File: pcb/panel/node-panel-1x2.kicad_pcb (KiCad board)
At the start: 4 copper layers, 64 x 108 mm, 325 parts, among them J1 LCD, J10 SPI, J13 Power, J14 SERIAL, J2 USB_C_USB2.0_16P, J3 INDICATOR, J4 GPB[0..3], J5 GPB[4..7], J7 GPA[4..7], J8 QWIIC1, J9 QWIIC2, Q1 MMBT2222A, SW1 RESET, SW2 BOOT, U1 ESP32-S3-WROOM-1-N8R2, U2 LM66200DRLR, U3 USBLC6-2P6, U4 MCP23017_ML, U5 LD1117S33TR_SOT223

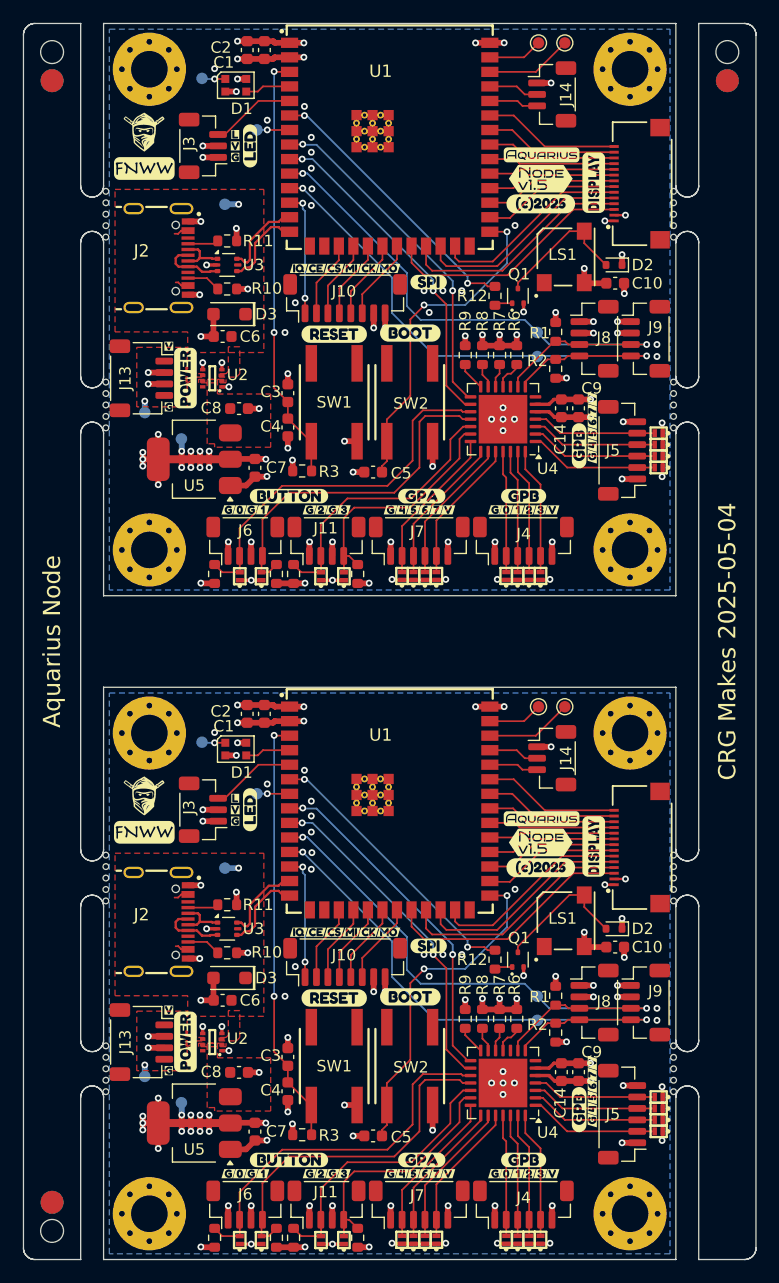
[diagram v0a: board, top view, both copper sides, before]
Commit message: Change panel to be 1x1
Changed connectors be vertical rather than horizontal.
Updated TVS diodes to DFN1006 rather than SMF
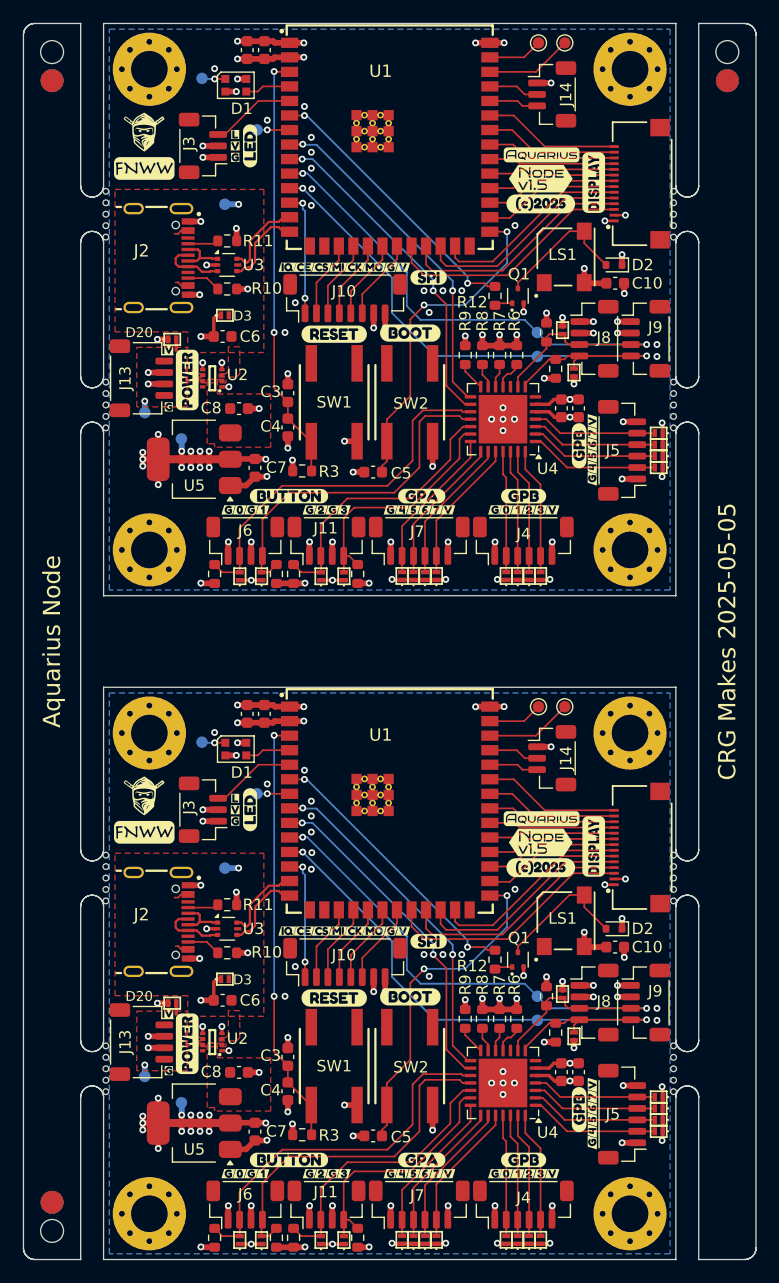
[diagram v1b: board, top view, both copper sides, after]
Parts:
- removed the D3 at (134.5, 45.4)
- removed the D3 at (134.5, 103.4)
- removed the R1 at (163.0, 47.0)
- removed the R1 at (163.0, 105.0)
- removed the kibuzzard-67B9F9C2 at (164.0, 46.7)
- removed the kibuzzard-67B9F9C2 at (164.0, 104.7)
- removed the kibuzzard-67B9F9CD at (164.0, 48.9)
- removed the kibuzzard-67B9F9CD at (164.0, 106.9)
- removed the kibuzzard-680D01D7 at (151.9, 42.6)
- removed the kibuzzard-680D01D7 at (151.9, 100.6)
- removed the kibuzzard-68103456 at (132.4, 26.3)
- removed the kibuzzard-68103456 at (132.4, 84.3)
- removed the kibuzzard-6810346D at (140.3, 27.9)
- removed the kibuzzard-6810346D at (140.3, 85.9)
- removed the kibuzzard-6810349E at (134.3, 34.4)
- removed the kibuzzard-6810349E at (134.3, 92.4)
- removed the kibuzzard-681034B6 at (130.4, 112.0)
- removed the kibuzzard-681034B6 at (130.4, 54.0)
- removed the kibuzzard-681035B7 at (133.1, 113.8)
- removed the kibuzzard-681035B7 at (133.1, 55.8)
- removed the kibuzzard-6812E37E at (142.1, 41.4)
- removed the kibuzzard-6812E37E at (142.1, 99.4)
- removed the kibuzzard-6812E3A0 at (143.7, 41.4)
- removed the kibuzzard-6812E3A0 at (143.7, 99.4)
- removed the kibuzzard-6812E3AD at (145.2, 99.4)
- removed the kibuzzard-6812E3AD at (145.2, 41.4)
- removed the kibuzzard-6812E3BB at (146.7, 41.4)
- removed the kibuzzard-6812E3BB at (146.7, 99.4)
- removed the kibuzzard-6812E3C5 at (148.4, 99.4)
- removed the kibuzzard-6812E3C5 at (148.4, 41.4)
- removed the kibuzzard-6812E420 at (140.6, 41.4)
- removed the kibuzzard-6812E420 at (140.6, 99.4)
- removed the kibuzzard-68142030 at (166.2, 111.8)
- removed the kibuzzard-68142030 at (166.2, 53.9)
- removed the kibuzzard-68142039 at (166.2, 112.8)
- removed the kibuzzard-68142039 at (166.2, 54.9)
- removed the kibuzzard-68142043 at (166.2, 113.8)
- removed the kibuzzard-68142043 at (166.2, 55.9)
- removed the kibuzzard-6814204F at (166.2, 56.9)
- removed the kibuzzard-6814204F at (166.2, 114.8)
- removed the kibuzzard-6814216F at (129.2, 106.2)
- removed the kibuzzard-6814216F at (129.2, 48.2)
- removed the kibuzzard-6815408B at (166.2, 115.8)
- removed the kibuzzard-6815408B at (166.2, 57.9)
- removed the kibuzzard-68154095 at (166.2, 110.8)
- removed the kibuzzard-68154095 at (166.2, 52.8)
- added D20: PESD5V5C1BL, CRGM Passive:DFN1006-2, F.Cu at (129.5, 105.6)
- added D20: PESD5V5C1BL, CRGM Passive:DFN1006-2, F.Cu at (129.5, 47.6)
- added D21: PESD3V3S1BL, CRGM Passive:DFN1006-2, F.Cu at (164.6, 50.5)
- added D21: PESD3V3S1BL, CRGM Passive:DFN1006-2, F.Cu at (164.6, 108.5)
- added D22: PESD3V3S1BL, CRGM Passive:DFN1006-2, F.Cu at (163.6, 46.8)
- added D22: PESD3V3S1BL, CRGM Passive:DFN1006-2, F.Cu at (163.6, 104.8)
- added D3: PESD5V5C1BL, CRGM Passive:DFN1006-2, F.Cu at (134.1, 45.5)
- added D3: PESD5V5C1BL, CRGM Passive:DFN1006-2, F.Cu at (134.1, 103.5)
- added R1: 10K, Resistor_SMD:R_0603_1608Metric, F.Cu at (162.2, 47.0)
- added R1: 10K, Resistor_SMD:R_0603_1608Metric, F.Cu at (162.2, 105.0)
- added kibuzzard-67B9F9C2: G***, kibuzzard-67B9F9C2, B.Cu at (164.1, 47.0)
- added kibuzzard-67B9F9C2: G***, kibuzzard-67B9F9C2, B.Cu at (164.1, 105.0)
- added kibuzzard-67B9F9CD: G***, kibuzzard-67B9F9CD, B.Cu at (163.9, 107.1)
- added kibuzzard-67B9F9CD: G***, kibuzzard-67B9F9CD, B.Cu at (163.9, 49.1)
- added kibuzzard-680D01D7: G***, kibuzzard-680D01D7, F.Cu at (151.9, 100.2)
- added kibuzzard-680D01D7: G***, kibuzzard-680D01D7, F.Cu at (151.9, 42.2)
- added kibuzzard-68103456: G***, kibuzzard-68103456, B.Cu at (132.1, 84.3)
- added kibuzzard-68103456: G***, kibuzzard-68103456, B.Cu at (132.1, 26.3)
- added kibuzzard-6810346D: G***, kibuzzard-6810346D, B.Cu at (134.8, 29.3)
- added kibuzzard-6810346D: G***, kibuzzard-6810346D, B.Cu at (134.8, 87.3)
- added kibuzzard-6810349E: G***, kibuzzard-6810349E, B.Cu at (134.1, 34.4)
- added kibuzzard-6810349E: G***, kibuzzard-6810349E, B.Cu at (134.1, 92.4)
- added kibuzzard-681034B6: G***, kibuzzard-681034B6, B.Cu at (130.1, 112.0)
- added kibuzzard-681034B6: G***, kibuzzard-681034B6, B.Cu at (130.1, 54.0)
- added kibuzzard-681035B7: G***, kibuzzard-681035B7, B.Cu at (132.8, 56.4)
- added kibuzzard-681035B7: G***, kibuzzard-681035B7, B.Cu at (132.8, 114.3)
- added kibuzzard-6812E37E: G***, kibuzzard-6812E37E, F.Cu at (141.0, 99.3)
- added kibuzzard-6812E37E: G***, kibuzzard-6812E37E, F.Cu at (141.0, 41.3)
- added kibuzzard-6812E3A0: G***, kibuzzard-6812E3A0, F.Cu at (142.6, 99.3)
- added kibuzzard-6812E3A0: G***, kibuzzard-6812E3A0, F.Cu at (142.6, 41.3)
- added kibuzzard-6812E3AD: G***, kibuzzard-6812E3AD, F.Cu at (144.0, 99.3)
- added kibuzzard-6812E3AD: G***, kibuzzard-6812E3AD, F.Cu at (144.0, 41.3)
- added kibuzzard-6812E3BB: G***, kibuzzard-6812E3BB, F.Cu at (145.4, 41.3)
- added kibuzzard-6812E3BB: G***, kibuzzard-6812E3BB, F.Cu at (145.4, 99.3)
- added kibuzzard-6812E3C5: G***, kibuzzard-6812E3C5, F.Cu at (147.2, 99.3)
- added kibuzzard-6812E3C5: G***, kibuzzard-6812E3C5, F.Cu at (147.2, 41.3)
- added kibuzzard-6812E420: G***, kibuzzard-6812E420, F.Cu at (139.6, 41.3)
- added kibuzzard-6812E420: G***, kibuzzard-6812E420, F.Cu at (139.6, 99.3)
- added kibuzzard-68142030: G***, kibuzzard-68142030, F.Cu at (166.2, 55.8)
- added kibuzzard-68142030: G***, kibuzzard-68142030, F.Cu at (166.2, 113.8)
- added kibuzzard-68142039: G***, kibuzzard-68142039, F.Cu at (166.2, 56.8)
- added kibuzzard-68142039: G***, kibuzzard-68142039, F.Cu at (166.2, 114.8)
- added kibuzzard-68142043: G***, kibuzzard-68142043, F.Cu at (166.2, 115.8)
- added kibuzzard-68142043: G***, kibuzzard-68142043, F.Cu at (166.2, 57.8)
- added kibuzzard-6814204F: G***, kibuzzard-6814204F, F.Cu at (166.2, 58.8)
- added kibuzzard-6814204F: G***, kibuzzard-6814204F, F.Cu at (166.2, 116.8)
- added kibuzzard-6814216F: G***, kibuzzard-6814216F, F.Cu at (129.2, 106.5)
- added kibuzzard-6814216F: G***, kibuzzard-6814216F, F.Cu at (129.2, 48.5)
- added kibuzzard-6815408B: G***, kibuzzard-6815408B, F.Cu at (166.2, 117.8)
- added kibuzzard-6815408B: G***, kibuzzard-6815408B, F.Cu at (166.2, 59.8)
- added kibuzzard-68154095: G***, kibuzzard-68154095, F.Cu at (166.2, 112.8)
- added kibuzzard-68154095: G***, kibuzzard-68154095, F.Cu at (166.2, 54.8)
- added kibuzzard-68194F3F: G***, kibuzzard-68194F3F, F.Cu at (148.6, 99.3)
- added kibuzzard-68194F3F: G***, kibuzzard-68194F3F, F.Cu at (148.6, 41.3)
- added kibuzzard-68194F50: G***, kibuzzard-68194F50, F.Cu at (149.7, 99.3)
- added kibuzzard-68194F50: G***, kibuzzard-68194F50, F.Cu at (149.7, 41.3)
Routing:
- net Board_1-GND: track 83.6 -> 86.0 mm, vias 72 -> 75
- net Board_0-GND: track 83.6 -> 86.0 mm, vias 72 -> 75
- net Board_1-I2C_SDA: track 52.6 -> 53.9 mm
- net Board_0-I2C_SDA: track 52.6 -> 53.9 mm
- net Board_1-I2C_SCL: track 51.1 -> 52.3 mm
- net Board_0-I2C_SCL: track 51.1 -> 52.3 mm
- net Board_1-LINE_5V: track 1.00 -> 1.95 mm
- net Board_0-LINE_5V: track 1.00 -> 1.95 mm
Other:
- board text added: "CRG Makes 2025-05-05"
- board text removed: "CRG Makes 2025-05-04"
